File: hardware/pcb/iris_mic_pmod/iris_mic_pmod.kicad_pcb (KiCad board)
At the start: 2 copper layers, 30 x 22 mm, 5 parts, among them J1 PMOD_2x6, U1 SPH0645LM4H

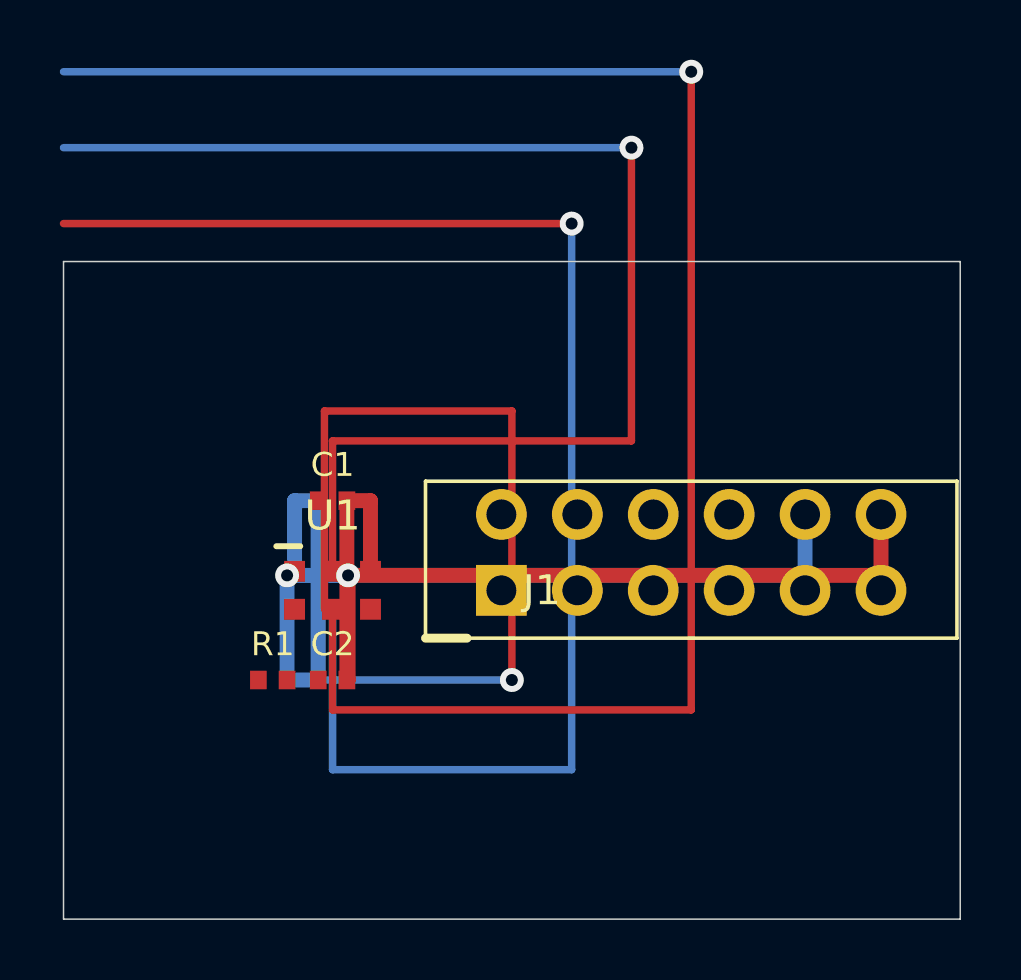
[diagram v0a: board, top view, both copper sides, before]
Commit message: feat(hardware/pcb): route pmod board, export gerbers, add DRC reports
- Updated schematic: bidir global labels for I2S_DATA/CLK/WS, added
  second pmod connector net stubs, replaced L_R net label with GND power
  symbol on mic L/R select pin
- PCB: updated copper pour and track layout post-route
- Exported full gerber set (F/B Cu, F/B Mask, F/B Silk, Edge, drill)
- Added DRC reports — 15 violations (shorting + clearance) still open

Co-Authored-By: Claude Sonnet 4.6 <noreply@anthropic.com>
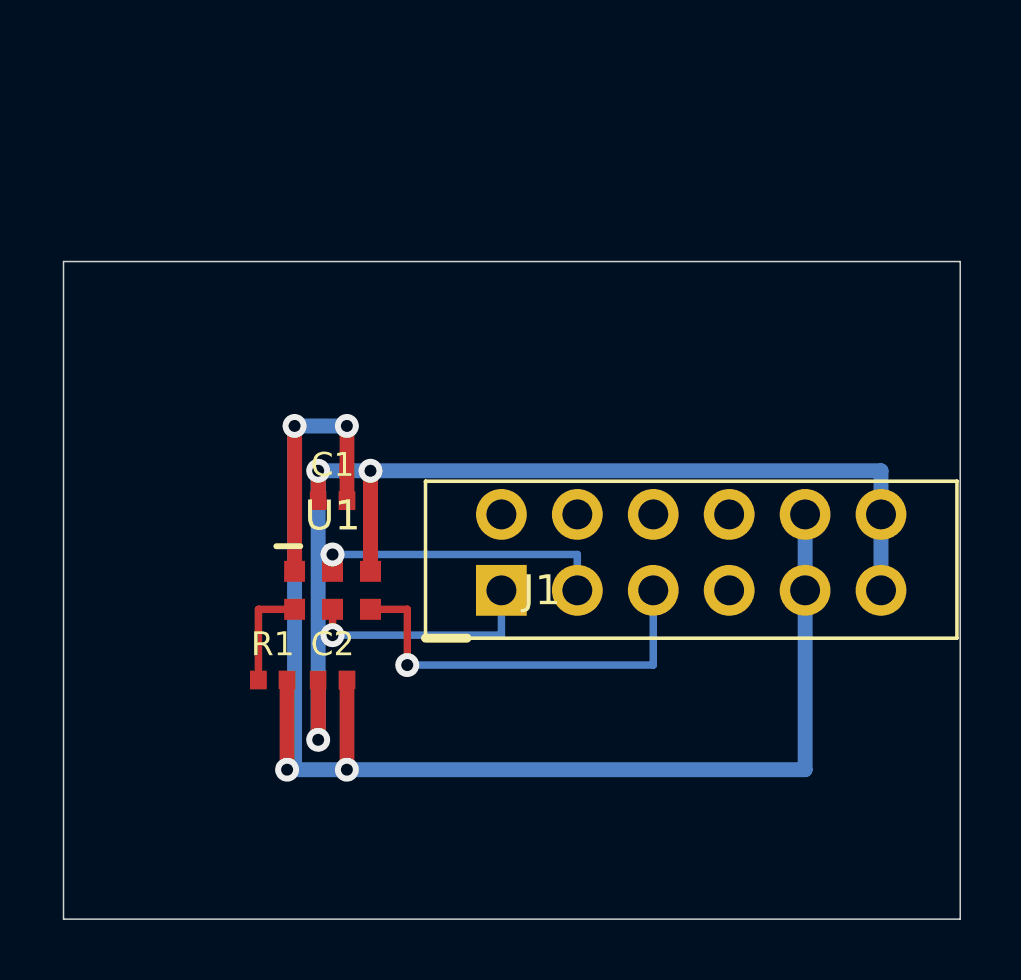
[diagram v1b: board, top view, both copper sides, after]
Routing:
- net I2S_DATA: track 57.7 -> 8.02 mm
- net I2S_WS: track 48.6 -> 13.8 mm
- net I2S_CLK: track 43.2 -> 9.96 mm
- net L_R: track 29.4 -> 3.58 mm, vias 1 -> 0
- net GND: track 34.1 -> 52.5 mm, vias 3 -> 4
- net +3V3: track 33.6 -> 38.2 mm
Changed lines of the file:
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@@
   (gr_text "2L 1.6mm FR4 ENIG" (at 1 3.2) (layer "Cmts.User")
     (effects (font (size 0.8 0.8) (thickness 0.1))))
-  (segment (start 7.73 10.365) (end 7.73 8) (width 0.5) (layer "B.Cu") (net 1))
-  (segment (start 7.73 8) (end 8.52 8) (width 0.5) (layer "B.Cu") (net 1))
-  (segment (start 8.52 8) (end 8.52 14) (width 0.5) (layer "B.Cu") (net 1))
-  (segment (start 8.52 14) (end 7.48 14) (width 0.5) (layer "B.Cu") (net 1))
-  (segment (start 7.48 14) (end 7.48 10.5) (width 0.5) (layer "B.Cu") (net 1))
-  (via (at 7.48 10.5) (size 0.8) (drill 0.4) (layers "F.Cu" "B.Cu") (net 1))
-  (segment (start 7.48 10.5) (end 24.81 10.5) (width 0.5) (layer "B.Cu") (net 1))
-  (segment (start 24.81 10.5) (end 24.81 11) (width 0.5) (layer "B.Cu") (net 1))
-  (via (at 24.81 11) (size 0.8) (drill 0.4) (layers "F.Cu" "B.Cu") (net 1))
+  (segment (start 7.73 10.365) (end 7.73 5.5) (width 0.5) (layer "F.Cu") (net 1))
+  (segment (start 9.48 8) (end 9.48 5.5) (width 0.5) (layer "F.Cu") (net 1))
+  (segment (start 7.48 14) (end 7.48 17.0) (width 0.5) (layer "F.Cu") (net 1))
+  (segment (start 9.48 14) (end 9.48 17.0) (width 0.5) (layer "F.Cu") (net 1))
+  (via (at 7.73 5.5) (size 0.8) (drill 0.4) (layers "F.Cu" "B.Cu") (net 1))
+  (via (at 9.48 5.5) (size 0.8) (drill 0.4) (layers "F.Cu" "B.Cu") (net 1))
+  (via (at 7.48 17.0) (size 0.8) (drill 0.4) (layers "F.Cu" "B.Cu") (net 1))
+  (via (at 9.48 17.0) (size 0.8) (drill 0.4) (layers "F.Cu" "B.Cu") (net 1))
+  (segment (start 7.73 5.5) (end 9.48 5.5) (width 0.5) (layer "B.Cu") (net 1))
+  (segment (start 7.73 5.5) (end 7.73 17.0) (width 0.5) (layer "B.Cu") (net 1))
+  (segment (start 7.48 17.0) (end 24.81 17.0) (width 0.5) (layer "B.Cu") (net 1))
+  (segment (start 24.81 17.0) (end 24.81 11) (width 0.5) (layer "B.Cu") (net 1))
   (segment (start 24.81 11) (end 24.81 8.46) (width 0.5) (layer "B.Cu") (net 1))
-  (via (at 24.81 8.46) (size 0.8) (drill 0.4) (layers "F.Cu" "B.Cu") (net 1))
-  (segment (start 10.27 10.365) (end 10.27 8) (width 0.5) (layer "F.Cu") (net 2))
-  (segment (start 10.27 8) (end 9.48 8) (width 0.5) (layer "F.Cu") (net 2))
-  (segment (start 9.48 8) (end 9.48 14) (width 0.5) (layer "F.Cu") (net 2))
-  (segment (start 9.48 14) (end 9.52 14) (width 0.5) (layer "F.Cu") (net 2))
-  (segment (start 9.52 14) (end 9.52 10.5) (width 0.5) (layer "F.Cu") (net 2))
-  (via (at 9.52 10.5) (size 0.8) (drill 0.4) (layers "F.Cu" "B.Cu") (net 2))
-  (segment (start 9.52 10.5) (end 27.35 10.5) (width 0.5) (layer "F.Cu") (net 2))
-  (segment (start 27.35 10.5) (end 27.35 11) (width 0.5) (layer "F.Cu") (net 2))
-  (via (at 27.35 11) (size 0.8) (drill 0.4) (layers "F.Cu" "B.Cu") (net 2))
-  (segment (start 27.35 11) (end 27.35 8.46) (width 0.5) (layer "F.Cu") (net 2))
-  (via (at 27.35 8.46) (size 0.8) (drill 0.4) (layers "F.Cu" "B.Cu") (net 2))
-  (segment (start 9 11.635) (end 9 15) (width 0.25) (layer "F.Cu") (net 3))
-  (segment (start 9 15) (end 21 15) (width 0.25) (layer "F.Cu") (net 3))
-  (segment (start 21 15) (end 21 -6.35) (width 0.25) (layer "F.Cu") (net 3))
-  (via (at 21 -6.35) (size 0.8) (drill 0.4) (layers "F.Cu" "B.Cu") (net 3))
-  (segment (start 21 -6.35) (end 0 -6.35) (width 0.25) (layer "B.Cu") (net 3))
-  (segment (start 9 10.365) (end 9 6) (width 0.25) (layer "F.Cu") (net 4))
-  (segment (start 9 6) (end 19 6) (width 0.25) (layer "F.Cu") (net 4))
-  (segment (start 19 6) (end 19 -3.81) (width 0.25) (layer "F.Cu") (net 4))
-  (via (at 19 -3.81) (size 0.8) (drill 0.4) (layers "F.Cu" "B.Cu") (net 4))
-  (segment (start 19 -3.81) (end 0 -3.81) (width 0.25) (layer "B.Cu") (net 4))
-  (segment (start 9 11.635) (end 9 17) (width 0.25) (layer "B.Cu") (net 5))
-  (segment (start 9 17) (end 17 17) (width 0.25) (layer "B.Cu") (net 5))
-  (segment (start 17 17) (end 17 -1.27) (width 0.25) (layer "B.Cu") (net 5))
-  (via (at 17 -1.27) (size 0.8) (drill 0.4) (layers "F.Cu" "B.Cu") (net 5))
-  (segment (start 17 -1.27) (end 0 -1.27) (width 0.25) (layer "F.Cu") (net 5))
-  (segment (start 8.73 11.635) (end 8.73 5) (width 0.25) (layer "F.Cu") (net 6))
-  (segment (start 8.73 5) (end 15 5) (width 0.25) (layer "F.Cu") (net 6))
-  (segment (start 15 5) (end 15 14) (width 0.25) (layer "F.Cu") (net 6))
-  (via (at 15 14) (size 0.8) (drill 0.4) (layers "F.Cu" "B.Cu") (net 6))
-  (segment (start 15 14) (end 7.48 14) (width 0.25) (layer "B.Cu") (net 6))
+  (segment (start 8.52 8) (end 8.52 7.0) (width 0.5) (layer "F.Cu") (net 2))
+  (segment (start 10.27 10.365) (end 10.27 7.0) (width 0.5) (layer "F.Cu") (net 2))
+  (segment (start 8.52 14) (end 8.52 16.0) (width 0.5) (layer "F.Cu") (net 2))
+  (via (at 8.52 7.0) (size 0.8) (drill 0.4) (layers "F.Cu" "B.Cu") (net 2))
+  (via (at 10.27 7.0) (size 0.8) (drill 0.4) (layers "F.Cu" "B.Cu") (net 2))
+  (via (at 8.52 16.0) (size 0.8) (drill 0.4) (layers "F.Cu" "B.Cu") (net 2))
+  (segment (start 8.52 7.0) (end 27.35 7.0) (width 0.5) (layer "B.Cu") (net 2))
+  (segment (start 27.35 7.0) (end 27.35 11) (width 0.5) (layer "B.Cu") (net 2))
+  (segment (start 8.52 7.0) (end 8.52 16.0) (width 0.5) (layer "B.Cu") (net 2))
+  (segment (start 9 11.635) (end 9 12.5) (width 0.25) (layer "F.Cu") (net 3))
+  (via (at 9 12.5) (size 0.8) (drill 0.4) (layers "F.Cu" "B.Cu") (net 3))
+  (segment (start 9 12.5) (end 14.65 12.5) (width 0.25) (layer "B.Cu") (net 3))
+  (segment (start 14.65 12.5) (end 14.65 11) (width 0.25) (layer "B.Cu") (net 3))
+  (segment (start 9 10.365) (end 9 9.8) (width 0.25) (layer "F.Cu") (net 4))
+  (via (at 9 9.8) (size 0.8) (drill 0.4) (layers "F.Cu" "B.Cu") (net 4))
+  (segment (start 9 9.8) (end 17.19 9.8) (width 0.25) (layer "B.Cu") (net 4))
+  (segment (start 17.19 9.8) (end 17.19 11) (width 0.25) (layer "B.Cu") (net 4))
+  (segment (start 10.27 11.635) (end 11.5 11.635) (width 0.25) (layer "F.Cu") (net 5))
+  (segment (start 11.5 11.635) (end 11.5 13.5) (width 0.25) (layer "F.Cu") (net 5))
+  (via (at 11.5 13.5) (size 0.8) (drill 0.4) (layers "F.Cu" "B.Cu") (net 5))
+  (segment (start 11.5 13.5) (end 19.73 13.5) (width 0.25) (layer "B.Cu") (net 5))
+  (segment (start 19.73 13.5) (end 19.73 11) (width 0.25) (layer "B.Cu") (net 5))
+  (segment (start 7.73 11.635) (end 6.52 11.635) (width 0.25) (layer "F.Cu") (net 6))
+  (segment (start 6.52 11.635) (end 6.52 14) (width 0.25) (layer "F.Cu") (net 6))
 )
